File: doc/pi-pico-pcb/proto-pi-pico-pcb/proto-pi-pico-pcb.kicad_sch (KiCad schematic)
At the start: 11 parts

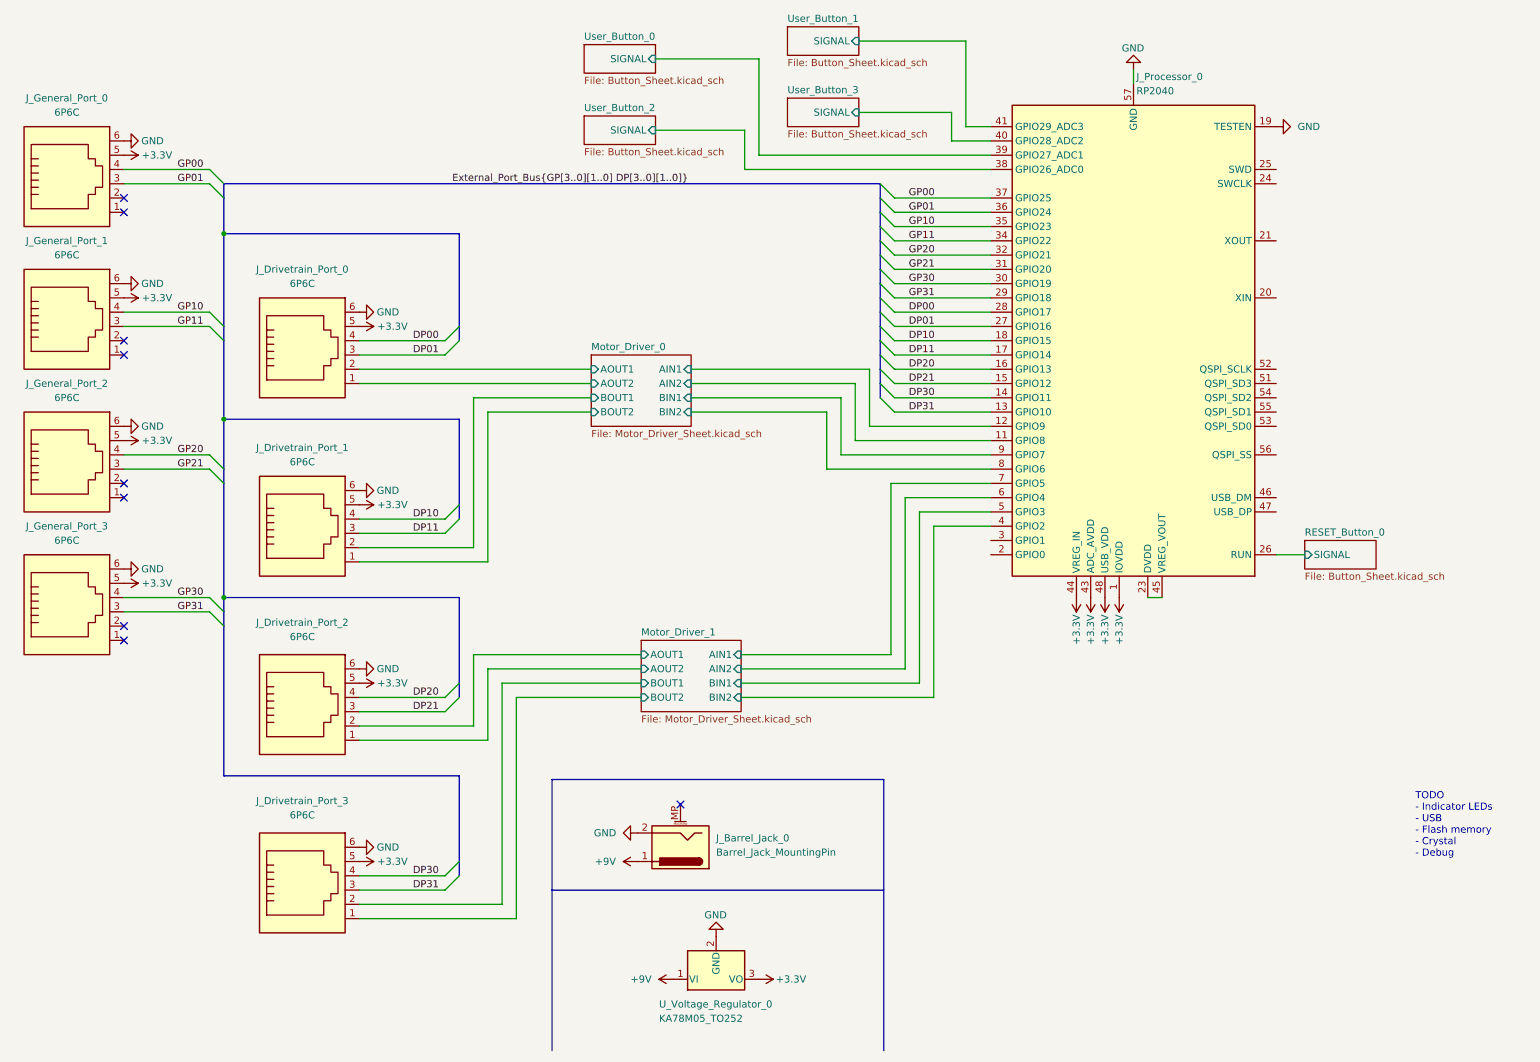
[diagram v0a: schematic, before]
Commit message: converted ports to nested sheets
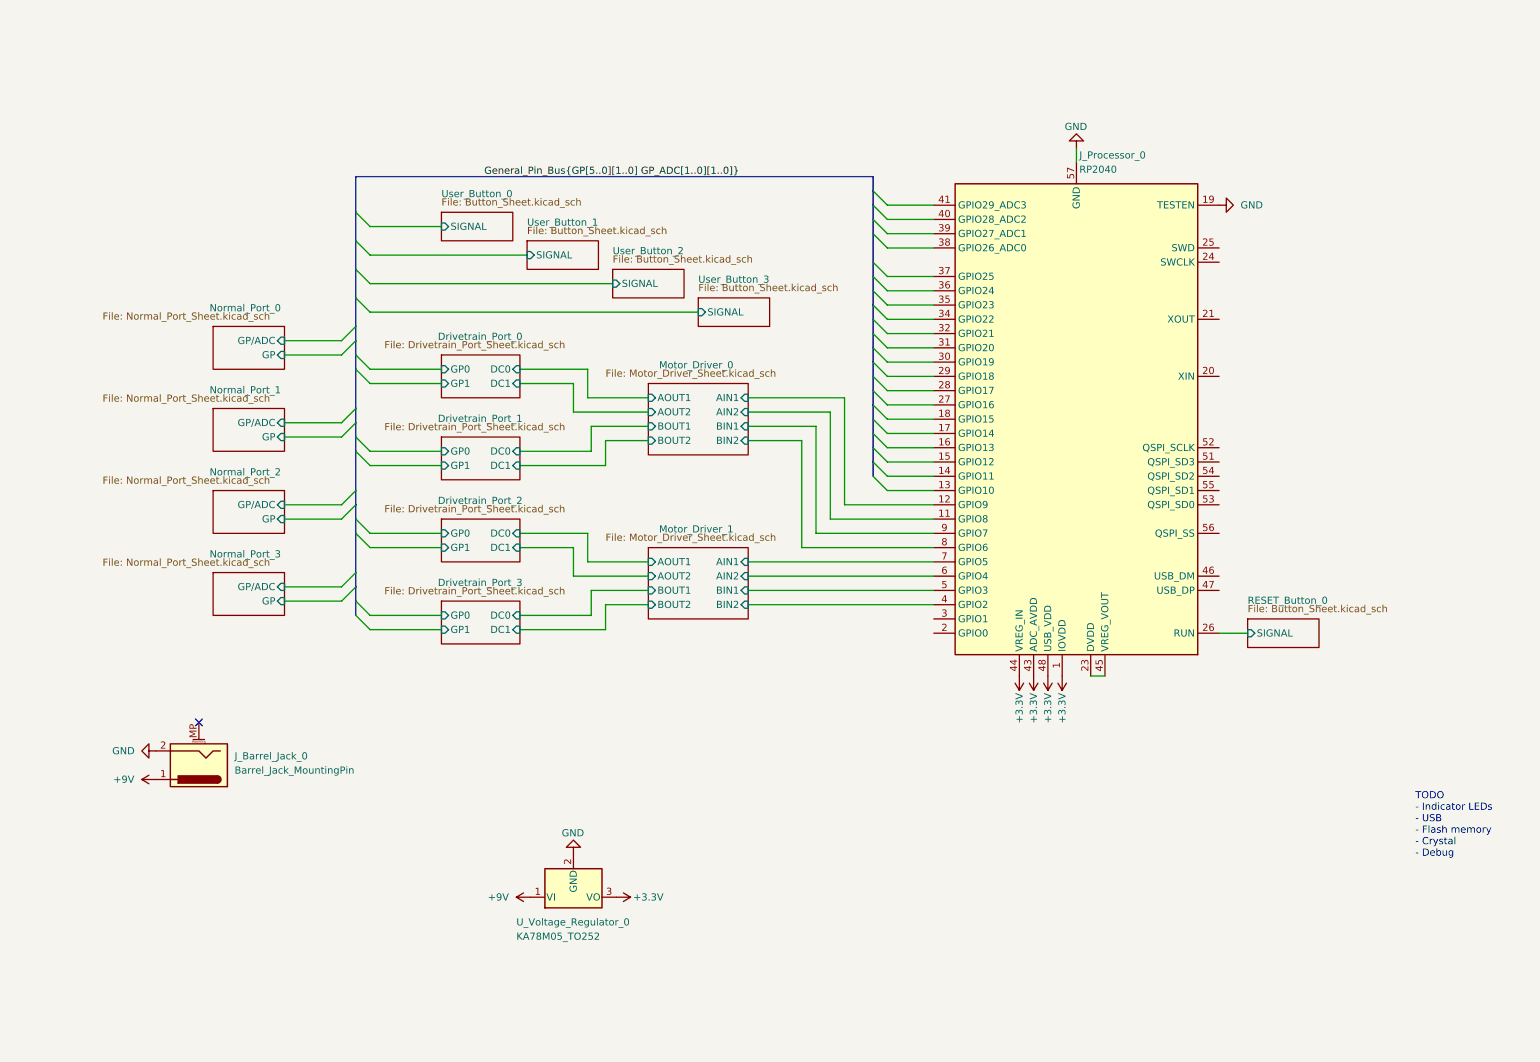
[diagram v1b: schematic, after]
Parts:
- removed J_Drivetrain_Port_0, J_Drivetrain_Port_1, J_Drivetrain_Port_2, J_Drivetrain_Port_3, J_General_Port_0, J_General_Port_1, J_General_Port_2, J_General_Port_3: 6P6C, Connector_RJ:RJ12_Amphenol_54601, symbol Connector:6P6C
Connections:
- net User_Button_0/SIGNAL: no longer J_Processor_0.39 (GPIO27_ADC1)
- net User_Button_1/SIGNAL: no longer J_Processor_0.41 (GPIO29_ADC3)
- net User_Button_2/SIGNAL: no longer J_Processor_0.38 (GPIO26_ADC0)
- net User_Button_3/SIGNAL: no longer J_Processor_0.40 (GPIO28_ADC2)
- net DP00: no longer names the net of J_Processor_0.28 (GPIO17)
- net DP01: no longer names the net of J_Processor_0.27 (GPIO16)
- net DP10: no longer names the net of J_Processor_0.18 (GPIO15)
- net DP11: no longer names the net of J_Processor_0.17 (GPIO14)
- net DP20: no longer names the net of J_Processor_0.16 (GPIO13)
- net DP21: no longer names the net of J_Processor_0.15 (GPIO12)
- net DP30: no longer names the net of J_Processor_0.14 (GPIO11)
- net DP31: no longer names the net of J_Processor_0.13 (GPIO10)
- net GP00: no longer names the net of J_Processor_0.37 (GPIO25)
- net GP01: no longer names the net of J_Processor_0.36 (GPIO24)
- net GP10: no longer names the net of J_Processor_0.35 (GPIO23)
- net GP11: no longer names the net of J_Processor_0.34 (GPIO22)
- net GP20: no longer names the net of J_Processor_0.32 (GPIO21)
- net GP21: no longer names the net of J_Processor_0.31 (GPIO20)
- net GP30: no longer names the net of J_Processor_0.30 (GPIO19)
- net GP31: no longer names the net of J_Processor_0.29 (GPIO18)
- no-connect marks 9 -> 1
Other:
- added sheet Drivetrain_Port_0 (Drivetrain_Port_Sheet.kicad_sch)
- added sheet Drivetrain_Port_1 (Drivetrain_Port_Sheet.kicad_sch)
- added sheet Drivetrain_Port_2 (Drivetrain_Port_Sheet.kicad_sch)
- added sheet Drivetrain_Port_3 (Drivetrain_Port_Sheet.kicad_sch)
- added sheet Normal_Port_0 (Normal_Port_Sheet.kicad_sch)
- added sheet Normal_Port_1 (Normal_Port_Sheet.kicad_sch)
- added sheet Normal_Port_2 (Normal_Port_Sheet.kicad_sch)
- added sheet Normal_Port_3 (Normal_Port_Sheet.kicad_sch)
- moved on the sheet: J_Barrel_Jack_0, J_Processor_0, U_Voltage_Regulator_0

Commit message: added flash memory
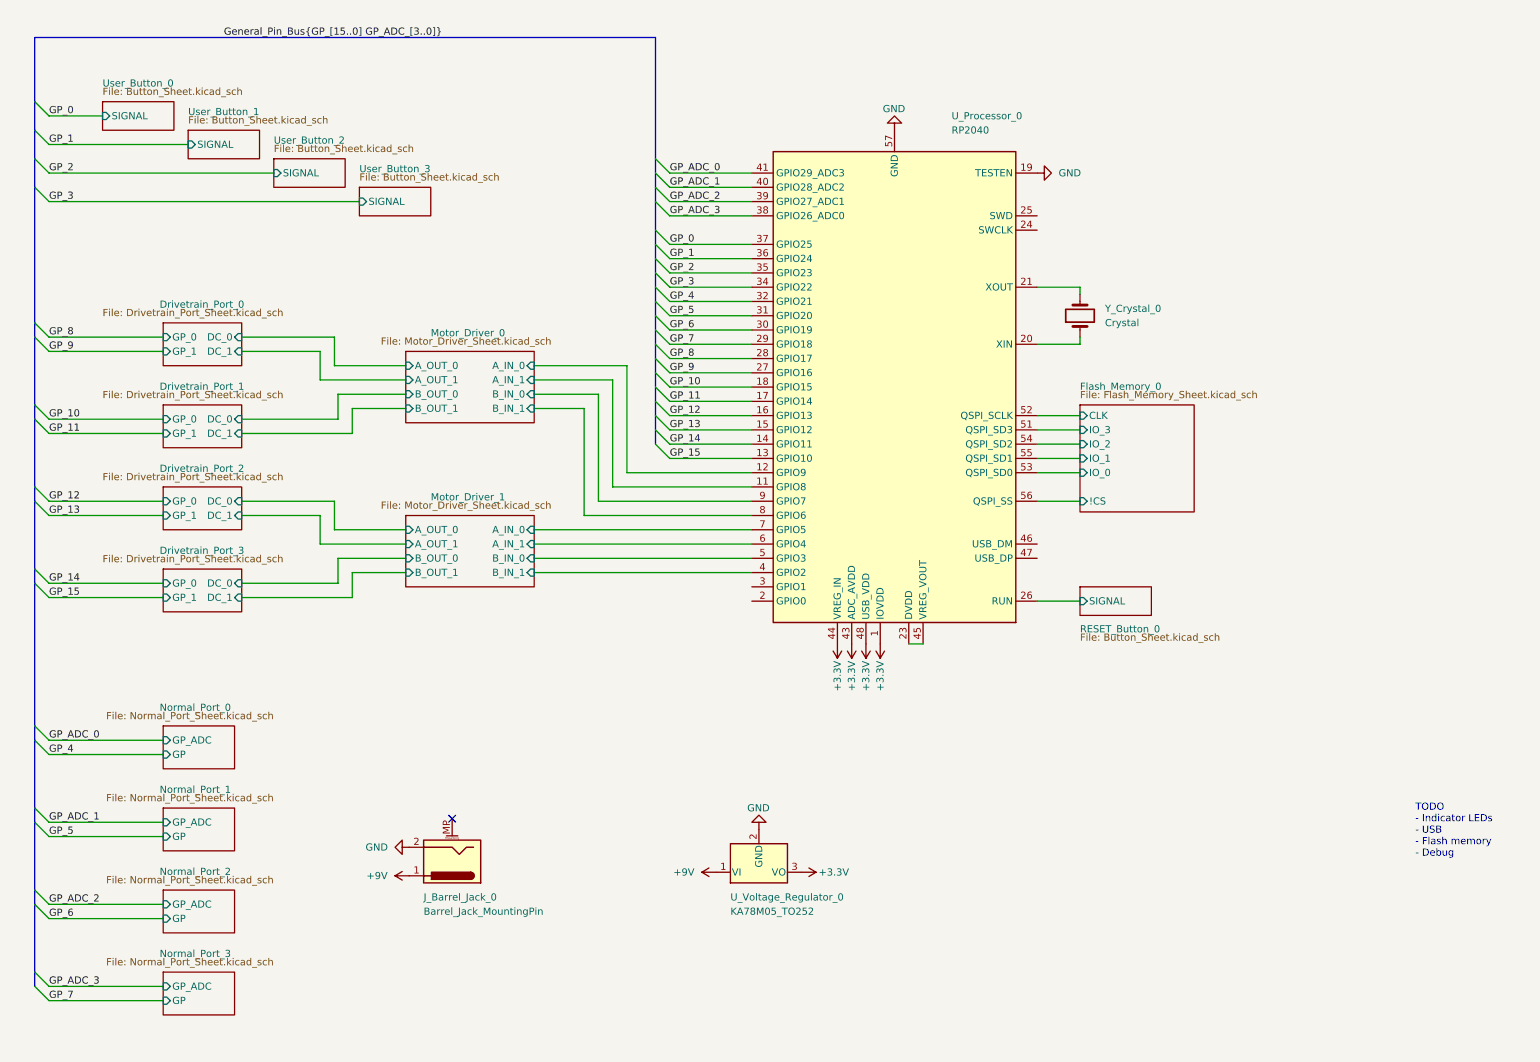
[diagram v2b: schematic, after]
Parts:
- added Y_Crystal_0: Crystal, Crystal:Crystal_SMD_Abracon_ABM8G-4Pin_3.2x2.5mm, symbol Device:Crystal
- renumbered J_Processor_0 to U_Processor_0
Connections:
- net GP_15: now reaches U_Processor_0.13 (GPIO10)
- net GP_14: now reaches U_Processor_0.14 (GPIO11)
- net GP_13: now reaches U_Processor_0.15 (GPIO12)
- net GP_12: now reaches U_Processor_0.16 (GPIO13)
- net GP_11: now reaches U_Processor_0.17 (GPIO14)
- net GP_10: now reaches U_Processor_0.18 (GPIO15)
- net at U_Processor_0.20 (XIN): now also Y_Crystal_0.1
- net at U_Processor_0.21 (XOUT): now also Y_Crystal_0.2
- net GP_9: now reaches U_Processor_0.27 (GPIO16)
- net GP_8: now reaches U_Processor_0.28 (GPIO17)
- net GP_7: now reaches U_Processor_0.29 (GPIO18)
- net GP_6: now reaches U_Processor_0.30 (GPIO19)
- net GP_5: now reaches U_Processor_0.31 (GPIO20)
- net GP_4: now reaches U_Processor_0.32 (GPIO21)
- net GP_3: now reaches U_Processor_0.34 (GPIO22)
- net GP_2: now reaches U_Processor_0.35 (GPIO23)
- net GP_1: now reaches U_Processor_0.36 (GPIO24)
- net GP_0: now reaches U_Processor_0.37 (GPIO25)
- net GP_ADC_3: now reaches U_Processor_0.38 (GPIO26_ADC0)
- net GP_ADC_2: now reaches U_Processor_0.39 (GPIO27_ADC1)
- net GP_ADC_1: now reaches U_Processor_0.40 (GPIO28_ADC2)
- net GP_ADC_0: now reaches U_Processor_0.41 (GPIO29_ADC3)
- net Flash_Memory_0/IO_3: now reaches U_Processor_0.51 (QSPI_SD3)
- net Flash_Memory_0/CLK: now reaches U_Processor_0.52 (QSPI_SCLK)
- net Flash_Memory_0/IO_0: now reaches U_Processor_0.53 (QSPI_SD0)
- net Flash_Memory_0/IO_2: now reaches U_Processor_0.54 (QSPI_SD2)
- net Flash_Memory_0/IO_1: now reaches U_Processor_0.55 (QSPI_SD1)
- net Flash_Memory_0/!CS: now reaches U_Processor_0.56 (QSPI_SS)
- net Motor_Driver_0/AIN1 renamed Motor_Driver_0/A_IN_0
- net Motor_Driver_0/AIN2 renamed Motor_Driver_0/A_IN_1
- net Motor_Driver_0/BIN1 renamed Motor_Driver_0/B_IN_0
- net Motor_Driver_0/BIN2 renamed Motor_Driver_0/B_IN_1
- net Motor_Driver_1/AIN1 renamed Motor_Driver_1/A_IN_0
- net Motor_Driver_1/AIN2 renamed Motor_Driver_1/A_IN_1
- net Motor_Driver_1/BIN1 renamed Motor_Driver_1/B_IN_0
- net Motor_Driver_1/BIN2 renamed Motor_Driver_1/B_IN_1
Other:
- added sheet Flash_Memory_0 (Flash_Memory_Sheet.kicad_sch)
- sheet Drivetrain_Port_0 ports: added DC_0, DC_1, GP_0, GP_1; removed DC0, DC1, GP0, GP1
- sheet Drivetrain_Port_1 ports: added DC_0, DC_1, GP_0, GP_1; removed DC0, DC1, GP0, GP1
- sheet Drivetrain_Port_2 ports: added DC_0, DC_1, GP_0, GP_1; removed DC0, DC1, GP0, GP1
- sheet Drivetrain_Port_3 ports: added DC_0, DC_1, GP_0, GP_1; removed DC0, DC1, GP0, GP1
- sheet Motor_Driver_0 ports: added A_IN_0, A_IN_1, A_OUT_0, A_OUT_1, B_IN_0, B_IN_1, B_OUT_0, B_OUT_1; removed AIN1, AIN2, AOUT1, AOUT2, BIN1, BIN2, BOUT1, BOUT2
- sheet Motor_Driver_1 ports: added A_IN_0, A_IN_1, A_OUT_0, A_OUT_1, B_IN_0, B_IN_1, B_OUT_0, B_OUT_1; removed AIN1, AIN2, AOUT1, AOUT2, BIN1, BIN2, BOUT1, BOUT2
- sheet Normal_Port_0 ports: added GP_ADC; removed GP/ADC
- sheet Normal_Port_1 ports: added GP_ADC; removed GP/ADC
- sheet Normal_Port_2 ports: added GP_ADC; removed GP/ADC
- sheet Normal_Port_3 ports: added GP_ADC; removed GP/ADC
- note added: "TODO - Indicator LEDs - USB - Flash memory - Debug"
- note removed: "TODO - Indicator LEDs - USB - Flash memory - Crystal - Debug"
- moved on the sheet: J_Barrel_Jack_0, U_Processor_0, U_Voltage_Regulator_0
